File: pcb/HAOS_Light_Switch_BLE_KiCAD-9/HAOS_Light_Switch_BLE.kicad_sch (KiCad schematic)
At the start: 38 parts, among them J1 GPIO, J2 GPIO, J3 GPIO, J4 Battery_CR2032, J5 PWR, J6 Conn_ARM_SWD_TagConnect_TC203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, J7 SWD, SW1 SW_Push, SW2 SW_Push, SW3 SW_Push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

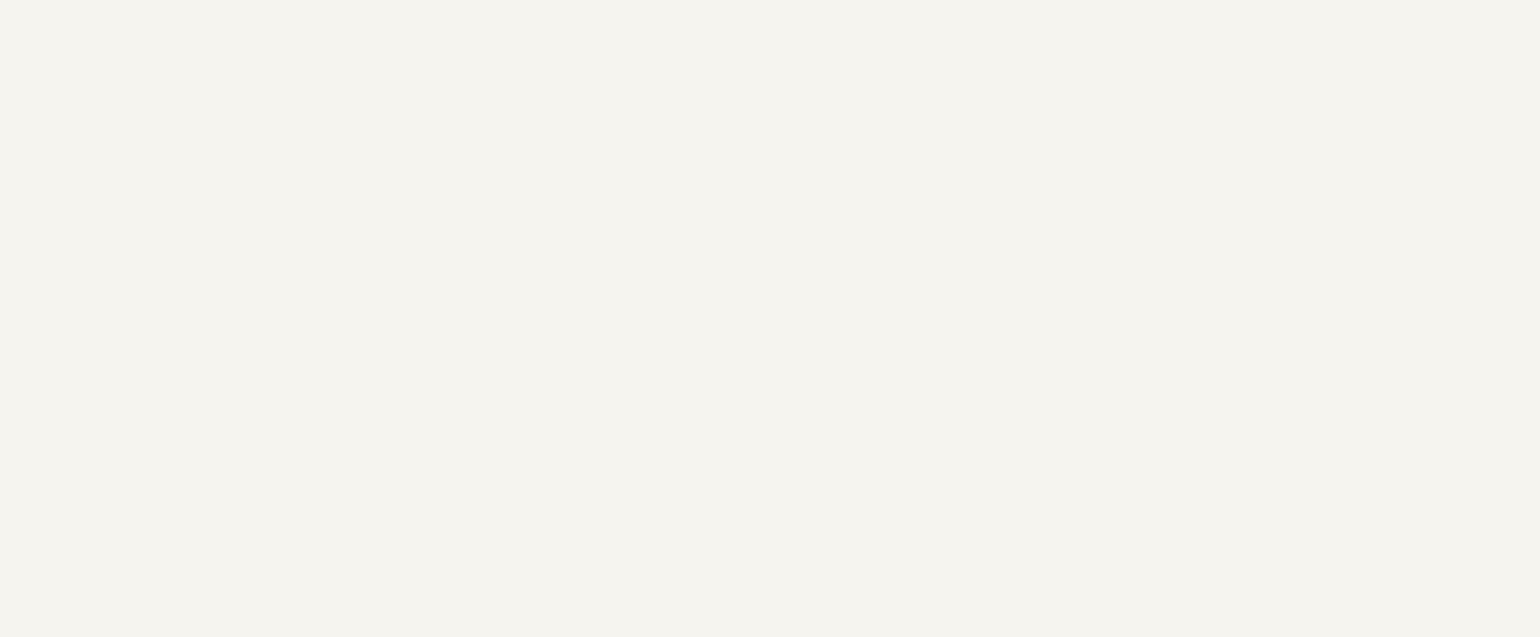
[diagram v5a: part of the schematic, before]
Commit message: added neutral current clamp draft copy of schematic.
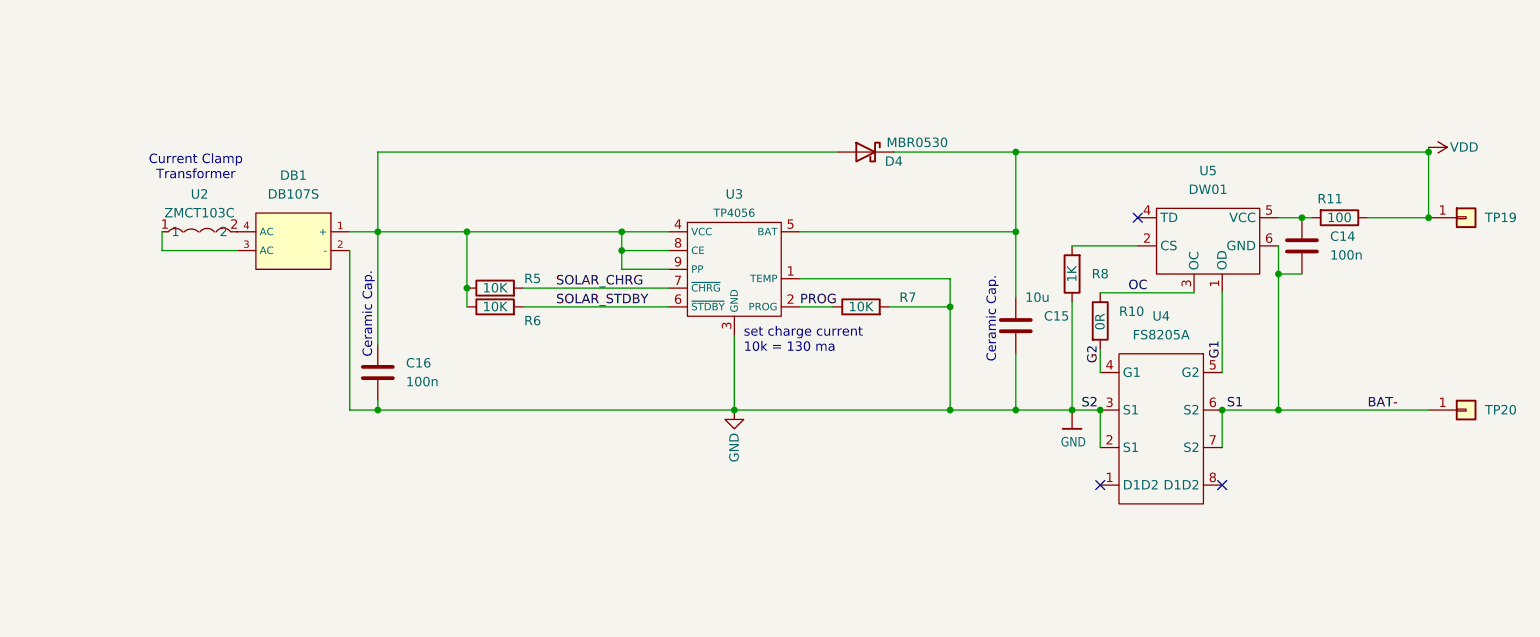
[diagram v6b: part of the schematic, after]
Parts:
- added C14, C16: 100n, Capacitor_SMD:C_0603_1608Metric, symbol Device:C
- added C15: 10u, Capacitor_SMD:C_0603_1608Metric, symbol Device:C
- added D4: MBR0530, Diode_SMD:D_SOD-123, symbol Diode:MBR0530
- added DB1: DB107S, PCM_JLCPCB:DBS_L8.2-W6.4-P5.10-LS10.0-BL, symbol PCM_JLCPCB-Diode-Packages:Bridge Rectifier, DB107S
- added R10: 0R, Resistor_SMD:R_0603_1608Metric, symbol Device:R
- added R11: 100, Resistor_SMD:R_0603_1608Metric, symbol Device:R
- added R5, R6, R7: 10K, Resistor_SMD:R_0603_1608Metric, symbol Device:R
- added R8: 1K, Resistor_SMD:R_0603_1608Metric, symbol Device:R
- added TP19, TP20: CONN_01, KICAD_Footprints:TST_x01_P2.54mm_Vertical, symbol Connector_Generic:Conn_01x01
- added U2: ZMCT103C, easyeda2kicad:XFMR-TH_ZMCT103C, symbol easyeda2kicad:ZMCT103C
- added U3: TP4056, KICAD_Footprints:SOIC-8-1EP_3.9x4.9mm_P1.27mm_EP2.29x3mm_Therm_Modified_for_JLCPCB, symbol KICAD_tp4056:TP4056
- added U4: FS8205A, KICAD_Footprints:TSSOP-8_4.4x3mm_P0.65mm_Modified_for_JLCPCB, symbol KICAD_fs8205a:FS8205A
- added U5: DW01, KICAD_Footprints:SOT-23-6_Modified_for_JLCPCB, symbol KICAD_dw01:DW01
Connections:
- net GND: now also C15.2, C16.2, DB1.2 (-), R7.2, R8.1, U3.1 (TEMP), U3.3 (GND), U4.2 (S1), U4.3 (S1)
- net VDD: now also C15.1, D4.1 (K), R11.1, TP19.1 (Pin_1), U3.5 (BAT)
- new net: C16.1, D4.2 (A), DB1.1 (+), R5.1, R6.1, U3.4 (VCC), U3.8 (CE), U3.9 (PP)
- new net: DB1.3 (AC), U2.1
- new net: DB1.4 (AC), U2.2
- new net: R8.2, U5.2 (CS)
- new net: C14.1, R11.2, U5.5 (VCC)
- new net BAT-: C14.2, TP20.1 (Pin_1), U4.6 (S2), U4.7 (S2), U5.6 (GND)
- new net G1: U4.5 (G2), U5.1 (OD)
- new net G2: R10.2, U4.4 (G1)
- new net OC: R10.1, U5.3 (OC)
- new net PROG: R7.1, U3.2 (PROG)
- new net SOLAR_CHRG: R5.2, U3.7 (~{CHRG})
- new net SOLAR_STDBY: R6.2, U3.6 (~{STDBY})
- no-connect marks 1 -> 4
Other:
- note added: "Ceramic Cap."
- note added: "Current Clamp Transformer"
- note added: "set charge current 10k = 130 ma"

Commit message: Draft AC power sniffer
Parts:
- removed DB1: DB107S, PCM_JLCPCB:DBS_L8.2-W6.4-P5.10-LS10.0-BL, symbol PCM_JLCPCB-Diode-Packages:Bridge Rectifier, DB107S
- added D5, D6, D7, D8: MBR0530, Diode_SMD:D_SOD-123, symbol Diode:MBR0530
- added R12, R9: 0R, Resistor_SMD:R_0603_1608Metric, symbol Device:R
- TP19, TP20: footprint KICAD_Footprints:TST_x01_P2.54mm_Vertical -> Connector_PinHeader_1.00mm:PinHeader_1x01_P1.00mm_Vertical
- U3: footprint KICAD_Footprints:SOIC-8-1EP_3.9x4.9mm_P1.27mm_EP2.29x3mm_Therm_Modified_for_JLCPCB -> easyeda2kicad:ESOP-8_L4.9-W3.9-P1.27-LS6.0-BL-EP
- U4: footprint KICAD_Footprints:TSSOP-8_4.4x3mm_P0.65mm_Modified_for_JLCPCB -> easyeda2kicad:TSSOP-8_L4.4-W3.0-P0.65-LS6.4-BL-2
- U5: footprint KICAD_Footprints:SOT-23-6_Modified_for_JLCPCB -> easyeda2kicad:SOT-23-6_L2.9-W1.6-P0.95-LS2.8-BL
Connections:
- net BAT-: now also R9.2
- net GND: now also D7.2 (A), D8.2 (A), R9.1
- net VDD: now also R12.2; no longer C15.1, D4.1 (K), R11.1, TP19.1 (Pin_1), U3.5 (BAT)
- net at C16.1, D4.2 (A), R5.1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: now also D5.1 (K), D6.1 (K)
- net at U2.1: now also D6.2 (A), D8.1 (K)
- net at U2.2: now also D5.2 (A), D7.1 (K)
- new net: C15.1, D4.1 (K), R11.1, R12.1, TP19.1 (Pin_1), U3.5 (BAT)
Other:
- note added: "Bypass jumper for low watts applicaitons. If powered by the CR2032, remove this 0R."
- note added: "Bypass jumper for low watts applicaitons. If powered by the wall, remove this 0R."
- note added: "DOWN"
- note added: "UP"
- moved on the sheet: AE1, C1, C10, C11, C12, C13, C14, C15, C16, C2, C3, C4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

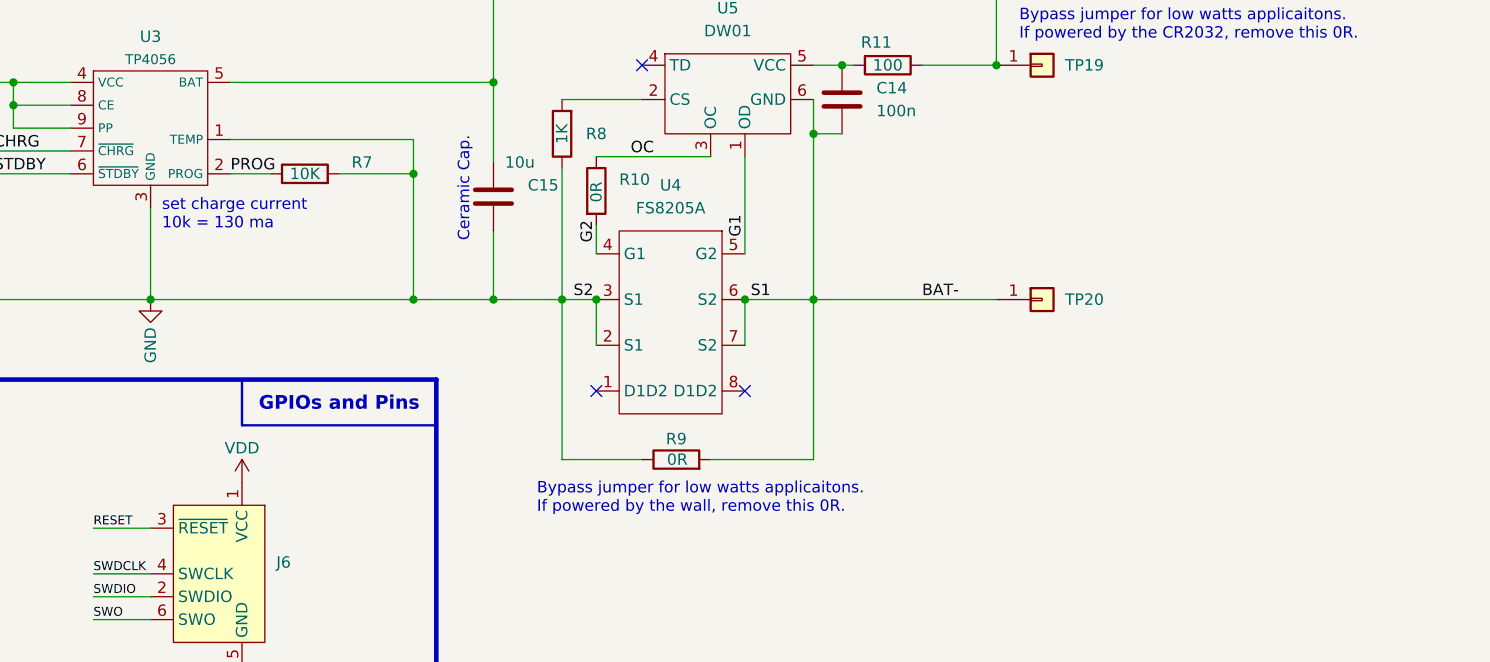
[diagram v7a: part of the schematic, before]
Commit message: Change R7 limiting charge current to 10ma for LIR2032 charging.
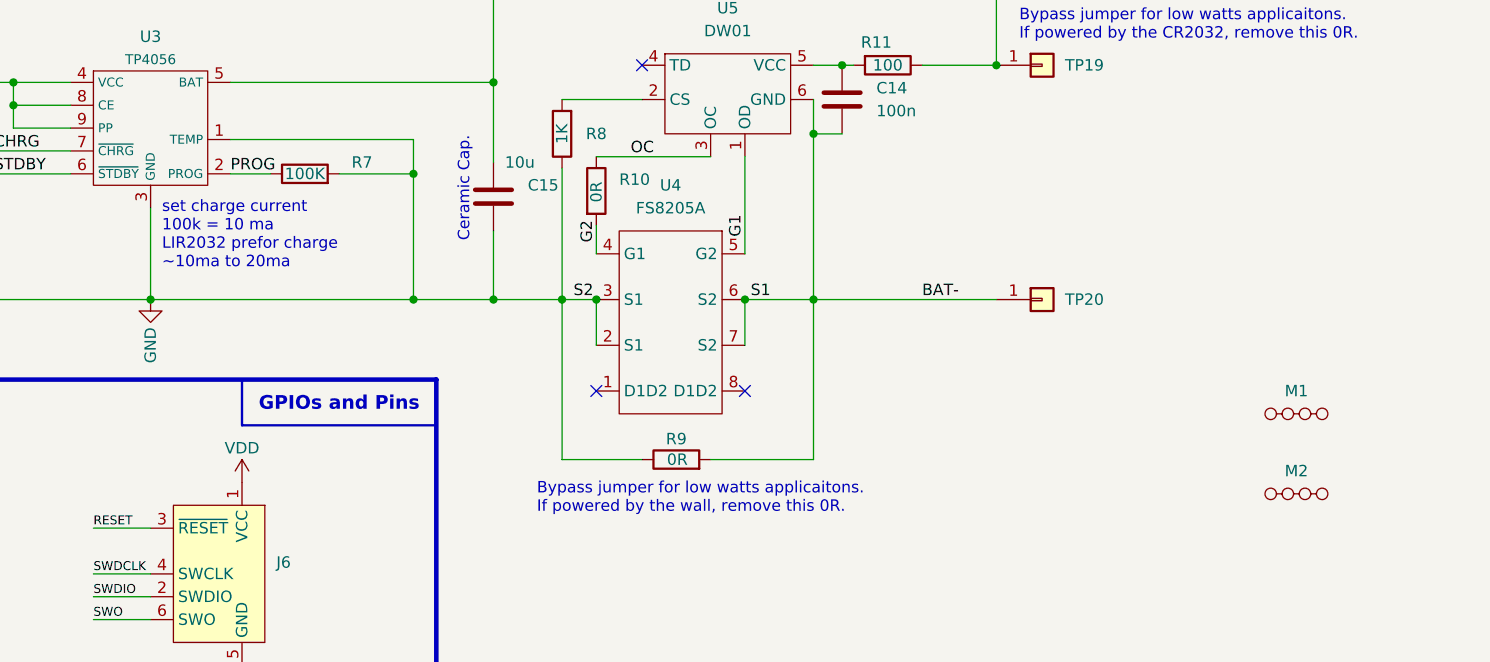
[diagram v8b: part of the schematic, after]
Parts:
- added M1, M2: ~, PCM_JLCPCB:MouseBites, Cosmetic, JLCPCB, 1.6mm, symbol PCM_JLCPCB-Manufacturing:Mousebites, Cosmetic, 3mm
- R7: value 10K -> 100K; LCSC C25804 -> C25803
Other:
- note added: "set charge current 100k = 10 ma LIR2032 prefor charge ~10ma to 20ma"
- note removed: "set charge current 10k = 130 ma"
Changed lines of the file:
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@@
 		)
 	)
-	(text "set charge current\n10k = 130 ma"
+	(text "set charge current\n100k = 10 ma\nLIR2032 prefor charge \n~10ma to 20ma"
 		(exclude_from_sim no)
-		(at 128.27 149.86 0)
+		(at 128.27 154.178 0)
 		(effects
 			(font
@@
 			)
 		)
-		(property "Value" "10K"
+		(property "Value" "100K"
 			(at 144.145 143.51 90)
 			(effects
@@
 			)
 		)
-		(property "LCSC" "C25804"
+		(property "LCSC" "C25803"
 			(at 144.145 143.51 0)
 			(effects
@@
 	)
 	(symbol
+		(lib_id "PCM_JLCPCB-Manufacturing:Mousebites, Cosmetic, 3mm")
+		(at 251.46 170.18 0)
+		(unit 1)
+		(exclude_from_sim no)
+		(in_bom yes)
+		(on_board yes)
+		(dnp no)
+		(fields_autoplaced yes)
+		(property "Reference" "M1"
+			(at 254.3175 167.64 0)
+			(effects
+				(font
+					(size 1.27 1.27)
+				)
+			)
+		)
+		(property "Value" "~"
+			(at 254.3175 167.64 0)
+			(effects
+				(font
+					(size 1.27 1.27)
+				)
+				(hide yes)
+			)
+		)
+		(property "Footprint" "PCM_JLCPCB:MouseBites, Cosmetic, JLCPCB, 1.6mm"
+			(at 251.46 170.18 0)
+			(effects
+				(font
+					(size 1.27 1.27)
+				)
+				(hide yes)
+			)
+		)
+		(property "Datasheet" "https://cdn.sparkfun.com/assets/home_page_posts/4/4/0/0/Mousebites_Whitepaper_Final.pdf"
+			(at 251.46 170.18 0)
+			(effects
+				(font
+					(size 1.27 1.27)
+				)
+				(hide yes)
+			)
+		)
+		(property "Description" "Breakaway Mousebites based on Sparkfun's recomended parameters tweaked for PCM_JLCPCB"
+			(at 251.46 170.18 0)
+			(effects
+				(font
+					(size 1.27 1.27)
+				)
+				(hide yes)
+			)
+		)
+		(instances
+			(project ""
+				(path "/7bf155d7-cf3f-4b19-a6e4-e06ff318c707"
+					(reference "M1")
+					(unit 1)
+				)
+			)
+		)
+	)
+	(symbol
 		(lib_id "PCM_JLCPCB-Crystals:Crystal, 32.768kHz, 13pF")
 		(at 44.45 59.69 90)
@@
 					(unit 1)
 				)
+			)
+		)
+	)
+	(symbol
+		(lib_id "PCM_JLCPCB-Manufacturing:Mousebites, Cosmetic, 3mm")
+		(at 251.46 179.07 0)
+		(unit 1)
+		(exclude_from_sim no)
+		(in_bom yes)
+		(on_board yes)
+		(dnp no)
+		(fields_autoplaced yes)
+		(property "Reference" "M2"
+			(at 254.3175 176.53 0)
+			(effects
+				(font
+					(size 1.27 1.27)
+				)
+			)
+		)
+		(property "Value" "~"
+			(at 254.3175 176.53 0)
+			(effects
+				(font
+					(size 1.27 1.27)
+				)
+				(hide yes)
+			)
+		)
+		(property "Footprint" "PCM_JLCPCB:MouseBites, Cosmetic, JLCPCB, 1.6mm"
+			(at 251.46 179.07 0)
+			(effects
+				(font
+					(size 1.27 1.27)
+				)
+				(hide yes)
+			)
+		)
+		(property "Datasheet" "https://cdn.sparkfun.com/assets/home_page_posts/4/4/0/0/Mousebites_Whitepaper_Final.pdf"
+			(at 251.46 179.07 0)
+			(effects
+				(font
+					(size 1.27 1.27)
+				)
+				(hide yes)
+			)
+		)
+		(property "Description" "Breakaway Mousebites based on Sparkfun's recomended parameters tweaked for PCM_JLCPCB"
+			(at 251.46 179.07 0)
+			(effects
+				(font
+					(size 1.27 1.27)
+				)
+				(hide yes)
+			)
+		)
+		(instances
+			(project "HAOS_Light_Switch_BLE"
+				(path "/7bf155d7-cf3f-4b19-a6e4-e06ff318c707"
+					(reference "M2")
+					(unit 1)
+				)
